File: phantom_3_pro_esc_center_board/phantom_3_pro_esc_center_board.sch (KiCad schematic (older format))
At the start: 57 parts, among them J1 CONN_BAT, J10 M1_BK, J11 M1_RD, J12 M1_YW, J13 M2_YW, J14 M2_RD, J15 M2_BK, J16 M3_BK, J17 M3_RD, J18 M3_YW, J19 M4_YW, J2 CONN_GPS, J20 M4_RD, J21 M4_BK, J3 CONN_GIMBAL, J4 CONN_CMPAS, J5 CONN_OFDM, J6 CONN_USB, J7 CONN_API, J8 CONN_MC_FRONT, J9 CONN_MC_BACK

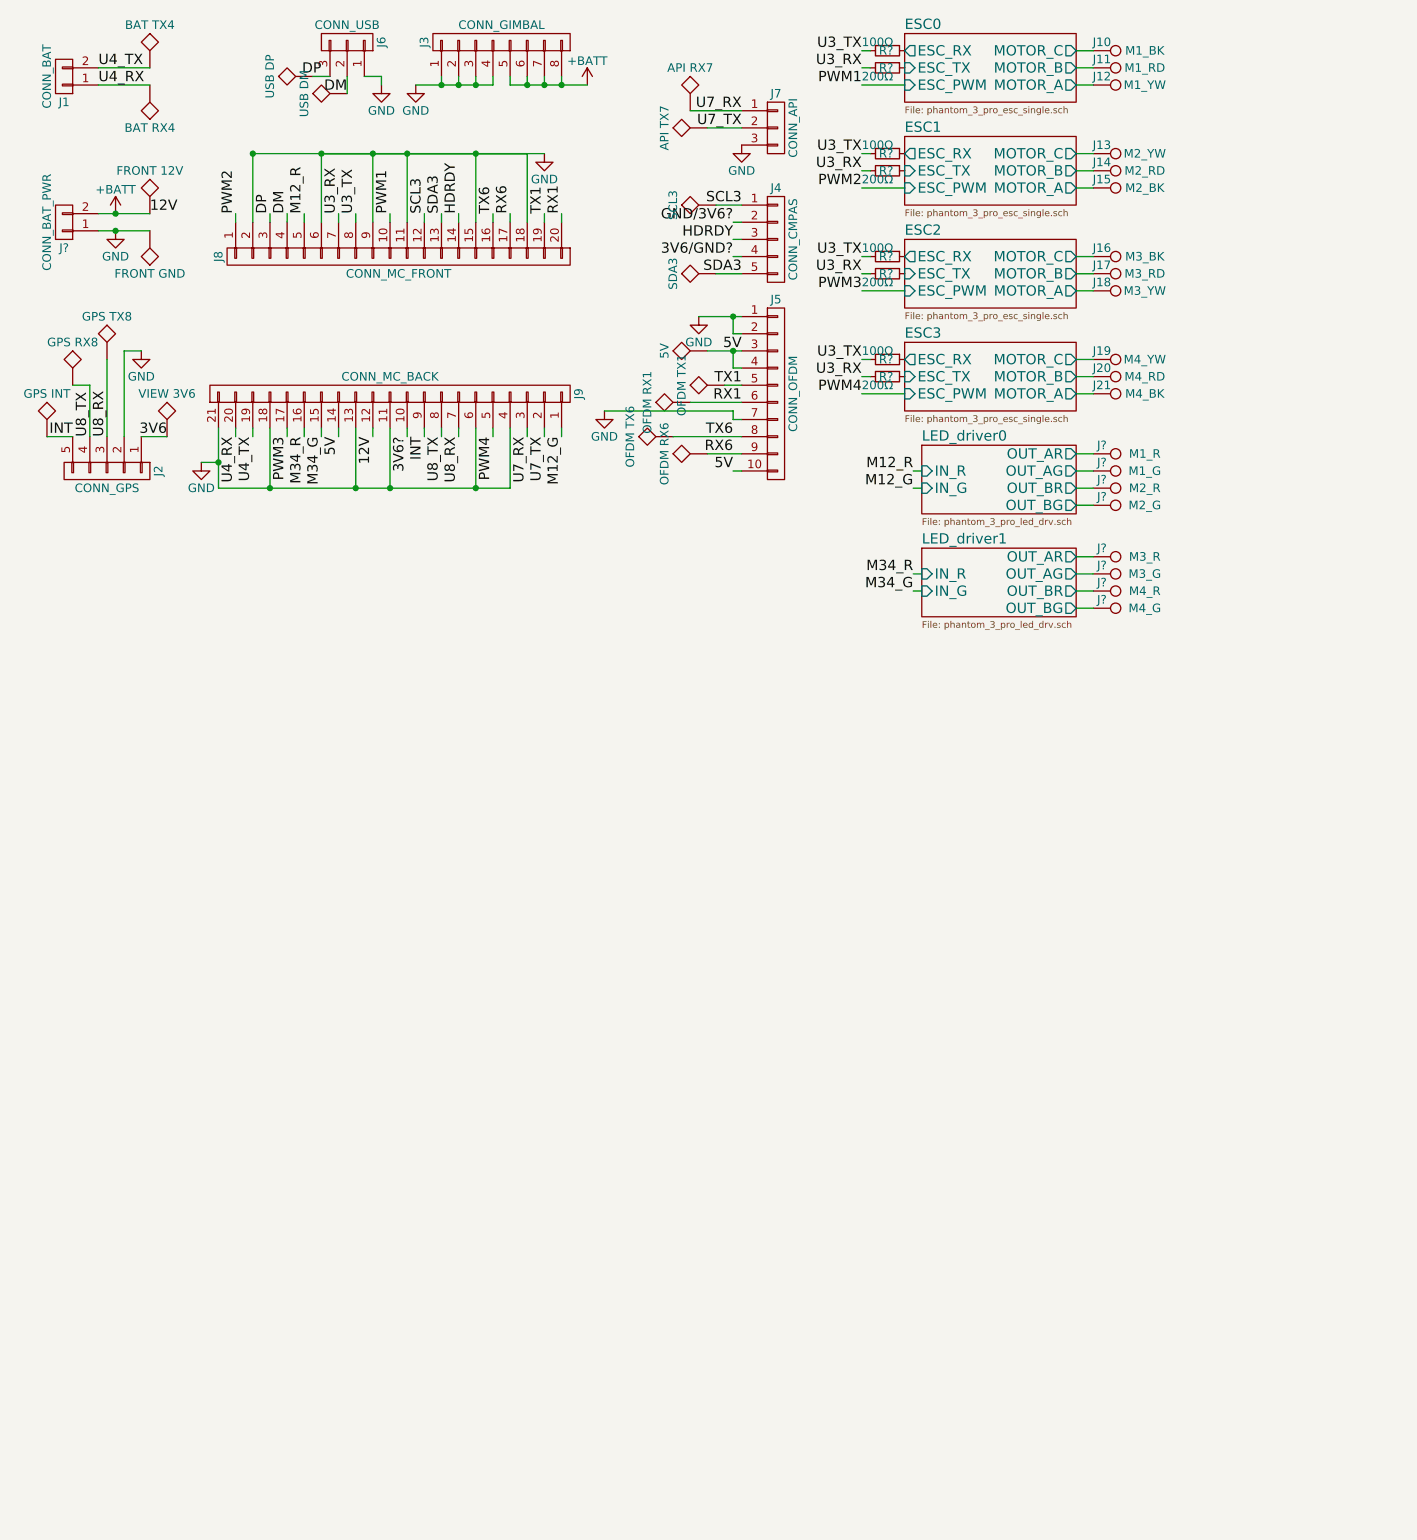
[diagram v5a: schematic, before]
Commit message: ESC Center: Added schematics of switching converters.
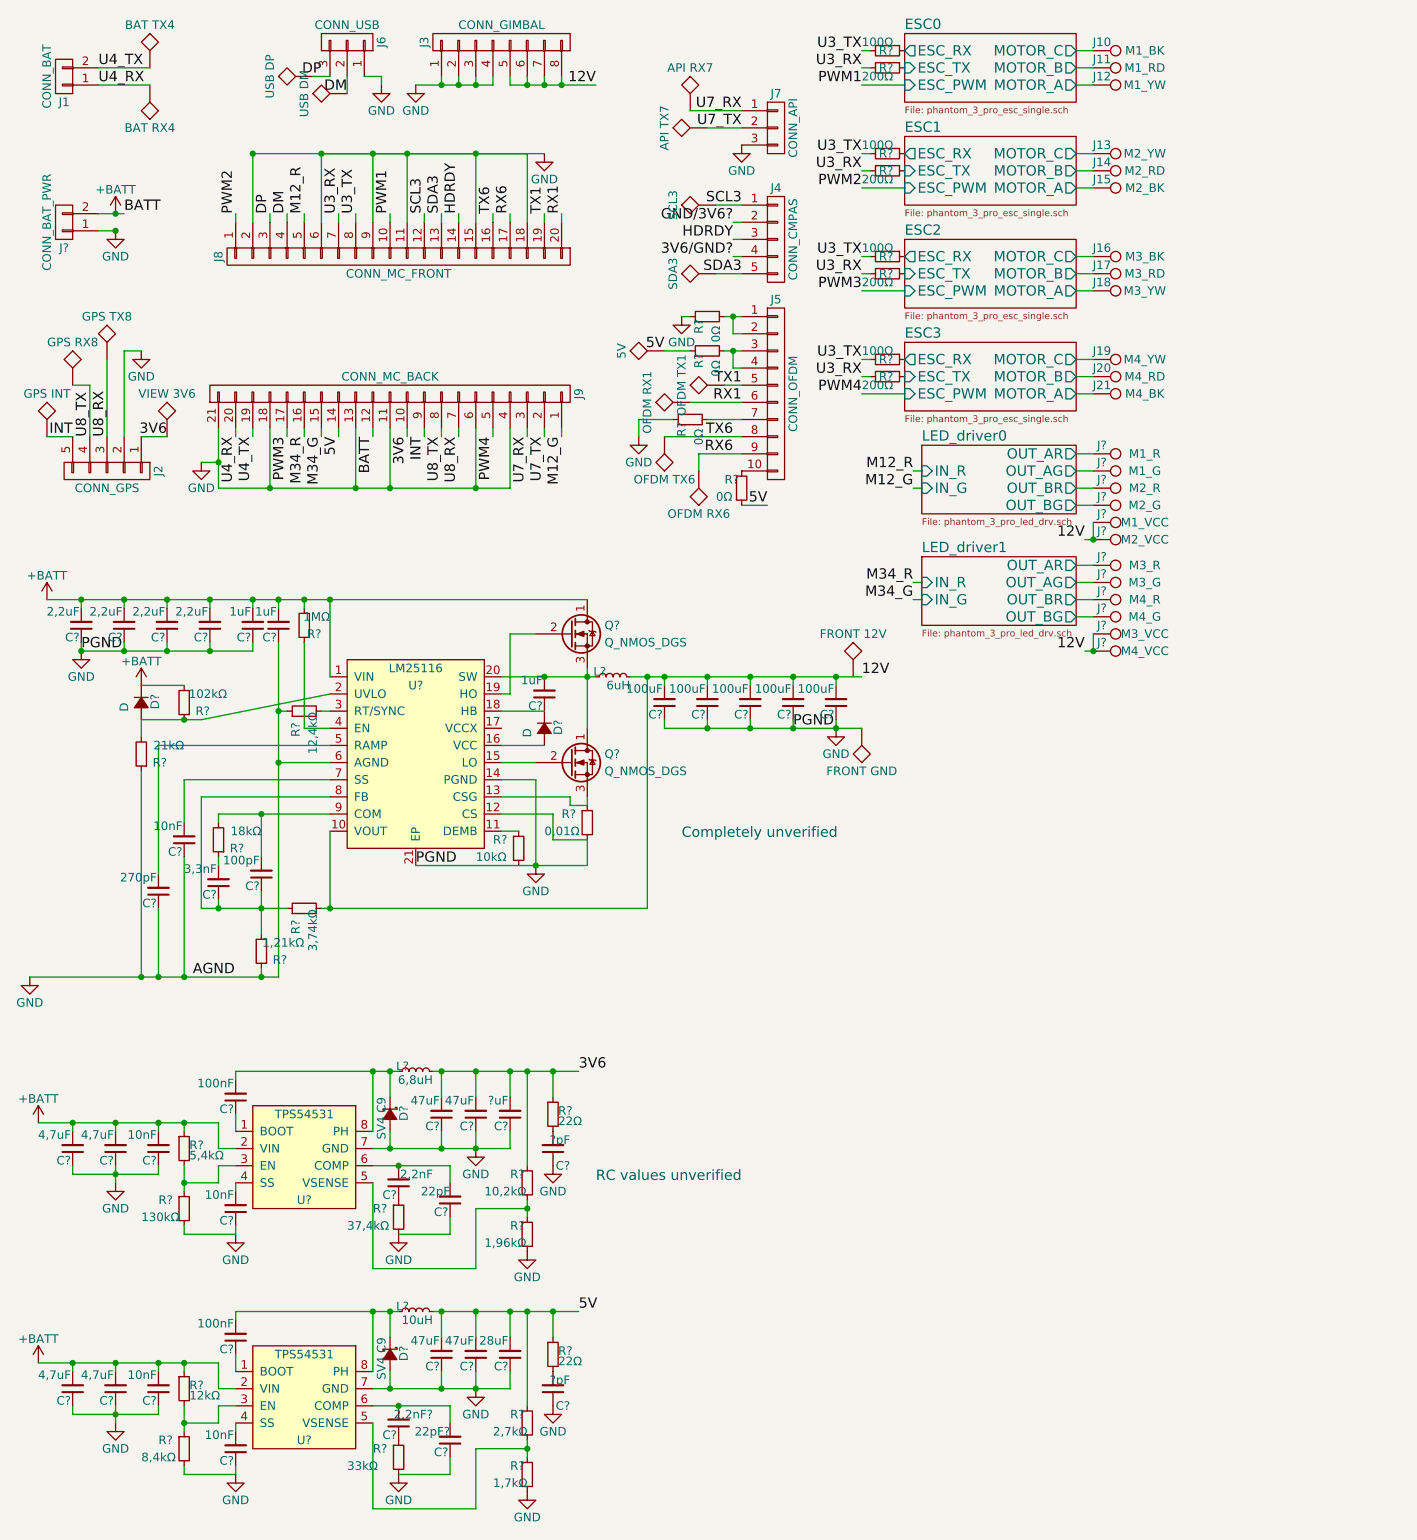
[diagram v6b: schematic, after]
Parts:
- removed TP?: FRONT 12V, symbol TEST
- removed TP?: FRONT GND, symbol TEST
- removed TP?: 5V, symbol TEST
- removed TP?: OFDM RX6, symbol TEST
- added C?: 2,2nF?, symbol C_Small
- added C? (x4): 47uF, symbol C_Small
- added C?: 28uF, symbol C_Small
- added C?: 100nF, meas. 96nF, symbol C_Small
- added C?: 10nF, meas 9.3nF, symbol C_Small
- added C? (x2): ?pF, symbol C_Small
- added C?: 22pF?, symbol C_Small
- added C? (x4): 4,7uF, symbol C_Small
- added C? (x4): 10nF, symbol C_Small
- added C? (x4): 2,2uF, symbol C_Small
- added C? (x3): 1uF, symbol C_Small
- added C? (x5): 100uF, symbol C_Small
- added C?: 100pF, symbol C_Small
- added C?: 3,3nF, symbol C_Small
- added C?: 270pF, symbol C_Small
- added C?: 2,2nF, symbol C_Small
- added C?: ?uF, symbol C_Small
- added C?: 100nF, symbol C_Small
- added C?: 22pF, symbol C_Small
- added D? (x2): SV4 C9, symbol D_Schottky_Small_ALT
- added D? (x2): D, symbol D_Small_ALT
- added J?: M1_VCC, symbol TEST_1P
- added J?: M2_VCC, symbol TEST_1P
- added J?: M3_VCC, symbol TEST_1P
- added J?: M4_VCC, symbol TEST_1P
- added L?: 10uH, symbol L_Small
- added L?: 6uH, symbol L_Small
- added L?: 6,8uH, symbol L_Small
- added Q? (x2): Q_NMOS_DGS, symbol Q_NMOS_DGS
- added R?: 12kΩ, symbol R_Small
- added R?: 8,4kΩ, symbol R_Small
- added R?: 1,7kΩ, symbol R_Small
- added R?: 2,7kΩ, symbol R_Small
- added R?: 33kΩ, symbol R_Small
- added R? (x2): 22Ω, symbol R_Small
- added R?: 1,21kΩ, symbol R_Small
- added R?: 3,74kΩ, symbol R_Small
- added R?: 18kΩ, symbol R_Small
- added R?: 1MΩ, symbol R_Small
- added R?: 12,4kΩ, symbol R_Small
- added R?: 102kΩ, symbol R_Small
- added R?: 21kΩ, symbol R_Small
- added R?: 0,01Ω, symbol R_Small
- added R?: 10kΩ, symbol R_Small
- added R?: 5,4kΩ, symbol R_Small
- added R?: 130kΩ, symbol R_Small
- added R?: 1,96kΩ, symbol R_Small
- added R?: 10,2kΩ, symbol R_Small
- added R?: 37,4kΩ, symbol R_Small
- added R? (x4): 0Ω, symbol R_Small
- added TP?: 5V, symbol TEST
- added TP?: OFDM RX6, symbol TEST
- added TP?: FRONT 12V, symbol TEST
- added TP?: FRONT GND, symbol TEST
- added U?: LM25116, symbol LM25116
- added U? (x2): TPS54531, symbol TPS54531
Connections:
- net 3V6? is gone; now on net 3V6: J9.10 (P10)
- net +BATT: now also C?.2, C?.2, C?.2, C?.2, C?.2, C?.2, C?.2, C?.2, C?.2, C?.2, C?.2, C?.2, D?.1 (K), Q?.1 (D), R?.1, R?.1, R?.2, R?.2, U?.1 (VIN), U?.2 (VIN), U?.2 (VIN); no longer J3.5 (P5), J3.6 (P6), J3.7 (P7), J3.8 (P8)
- net 3V6: now also C?.2, C?.2, C?.2, L?.2, R?.1, R?.1
- net 5V: now also C?.2, C?.2, C?.2, L?.2, R?.1, R?.1, R?.1, R?.2, TP?.1; no longer J5.10 (P10), J5.3 (P3), J5.4 (P4)
- net GND: now also C?.1, C?.1, C?.1, C?.1, C?.1, C?.1, C?.1, C?.1, C?.1, C?.1, C?.1, C?.1, C?.1, C?.1, C?.1, C?.1, C?.1, C?.1, C?.1, C?.1, C?.1, C?.1, C?.1, C?.1, C?.1, C?.1, C?.1, C?.1, C?.1, C?.1, C?.1, D?.2 (A), D?.2 (A), R?.1, R?.1, R?.1, R?.1, R?.1, R?.2, R?.2, R?.2, R?.2, R?.2, R?.2, R?.2, TP?.1, U?.12 (CS), U?.14 (PGND), U?.21 (EP), U?.6 (AGND), U?.7 (GND), U?.7 (GND); no longer J5.1 (P1), J5.2 (P2), J5.7 (P7)
- net RX6: now also TP?.1
- new net: J5.1 (P1), J5.2 (P2), R?.2
- new net: J5.10 (P10), R?.1
- new net: J5.3 (P3), J5.4 (P4), R?.2
- new net: J5.7 (P7), R?.2
- new net: R?.1, U?.11 (DEMB)
- new net: Q?.3 (S), R?.1, U?.13 (CSG)
- new net: Q?.2 (G), U?.15 (LO)
- new net: D?.2 (A), U?.16 (VCC)
- new net: C?.1, D?.1 (K), U?.18 (HB)
- new net: Q?.2 (G), U?.19 (HO)
- new net: D?.2 (A), R?.1, R?.2, U?.2 (UVLO)
- new net: C?.2, L?.1, Q?.1 (D), Q?.3 (S), U?.20 (SW)
- new net: R?.2, U?.3 (RT/SYNC)
- new net: R?.1, U?.4 (EN)
- new net: C?.2, U?.5 (RAMP)
- new net: C?.2, U?.7 (SS)
- new net: C?.1, C?.1, R?.1, R?.2, U?.8 (FB)
- new net: C?.2, R?.2, U?.9 (COM)
- new net: C?.1, U?.1 (BOOT) (x2)
- new net: R?.1, R?.2, U?.3 (EN) (x2)
- new net: C?.2, U?.4 (SS) (x2)
- new net: R?.1, R?.2, U?.5 (VSENSE) (x2)
- new net: C?.2, C?.2, U?.6 (COMP) (x2)
- new net: C?.2, D?.1 (K), L?.1, U?.8 (PH) (x2)
- new net: C?.1, R?.1 (x2)
- new net: C?.2, R?.2 (x2)
- new net: C?.2, R?.1
- new net 12V: C?.2, C?.2, C?.2, C?.2, C?.2, J3.5 (P5), J3.6 (P6), J3.7 (P7), J3.8 (P8), J?.1, J?.1, J?.1, J?.1, L?.2, R?.2, U?.10 (VOUT)
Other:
- note added: "Completely unverified"
- note added: "RC values unverified"
- moved on the sheet: J?

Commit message: Updated PDF exports.
The schematics exported to PDF were updated.
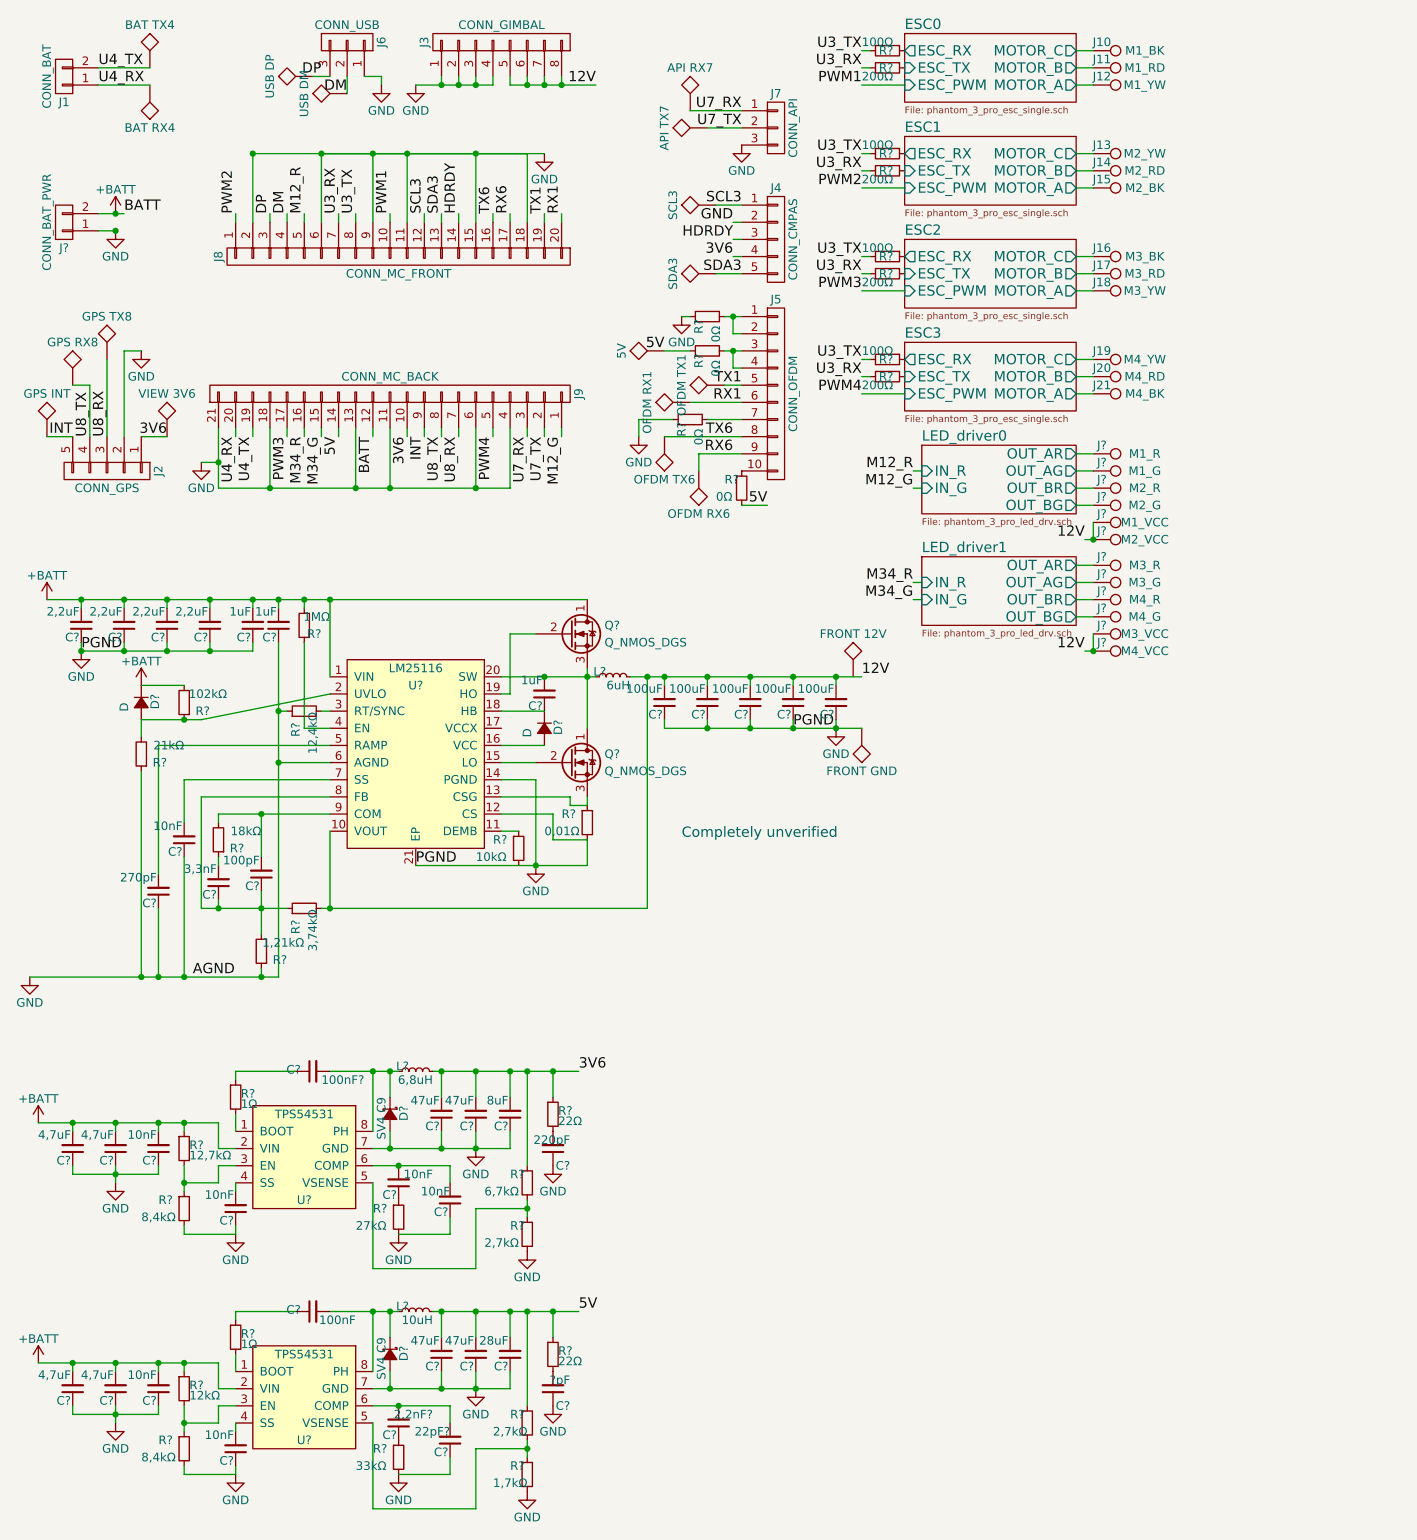
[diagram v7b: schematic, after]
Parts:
- added R? (x2): 1Ω, symbol R_Small
- C?: value 2,2nF -> 10nF
- C?: value ?uF -> 8uF
- C?: value 100nF -> 100nF?
- C?: value 22pF -> 10nF
- C?: value ?pF -> 220pF
- R?: value 5,4kΩ -> 12,7kΩ
- R?: value 130kΩ -> 8,4kΩ
- R?: value 1,96kΩ -> 2,7kΩ
- R?: value 10,2kΩ -> 6,7kΩ
- R?: value 37,4kΩ -> 27kΩ
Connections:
- net 3V6/GND? is gone; now on net 3V6: J4.4 (P4)
- net GND/3V6? is gone; now on net GND: J4.2 (P2)
- net at U?.1 (BOOT): now also R?.2; no longer C?.1
- net at C?.1: now also R?.1; no longer U?.1 (BOOT)
- new net: C?.1, R?.1
- new net: R?.2, U?.1 (BOOT)
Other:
- note removed: "RC values unverified"
- moved on the sheet: C?
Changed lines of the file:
@@
 $EndComp
 Text Label 4650 1700 2    60   ~ 0
-GND/3V6?
+GND
 Text Label 4650 1900 2    60   ~ 0
-3V6/GND?
+3V6
 $Comp
 L LM25116 U?
@@
 L C_Small C?
 U 1 1 597BBDD7
-P 1750 8200
-F 0 "C?" H 1760 8270 50  0000 L CNN
-F 1 "100nF" H 1760 8120 50  0000 L CNN
-F 2 "meas. 96nF" H 1750 8200 50  0001 C CNN
-F 3 "" H 1750 8200 50  0001 C CNN
-	1    1750 8200
-	-1   0    0    1
+P 2200 8050
+F 0 "C?" V 2210 8120 50  0000 L CNN
+F 1 "100nF" V 2150 7800 50  0000 L CNN
+F 2 "meas. 96nF" H 2200 8050 50  0001 C CNN
+F 3 "" H 2200 8050 50  0001 C CNN
+	1    2200 8050
+	0    -1   -1   0
 $EndComp
 $Comp
@@
 P 2700 8900
 F 0 "R?" H 2550 8950 50  0000 L CNN
-F 1 "33kΩ" H 2400 8850 50  0000 L CNN
+F 1 "33kΩ" H 2450 8850 50  0000 L CNN
 F 2 "" H 2700 8900 50  0001 C CNN
 F 3 "" H 2700 8900 50  0001 C CNN
@@
 	1750 8100 1750 8050
 Wire Wire Line
-	1750 8050 2700 8050
-Wire Wire Line
 	2550 8050 2550 8400
 Wire Wire Line
@@
 P 2700 7300
 F 0 "C?" H 2710 7370 50  0000 L CNN
-F 1 "2,2nF" H 2500 7250 50  0000 L CNN
+F 1 "10nF" H 2500 7250 50  0000 L CNN
 F 2 "" H 2700 7300 50  0001 C CNN
 F 3 "" H 2700 7300 50  0001 C CNN
@@
 P 3350 6900
 F 0 "C?" H 3360 6970 50  0000 L CNN
-F 1 "?uF" H 3360 6820 50  0000 L CNN
+F 1 "8uF" H 3360 6820 50  0000 L CNN
 F 2 "" H 3350 6900 50  0001 C CNN
 F 3 "" H 3350 6900 50  0001 C CNN
@@
 L C_Small C?
 U 1 1 59840470
-P 1750 6800
-F 0 "C?" H 1760 6870 50  0000 L CNN
-F 1 "100nF" H 1760 6720 50  0000 L CNN
-F 2 "" H 1750 6800 50  0001 C CNN
-F 3 "" H 1750 6800 50  0001 C CNN
-	1    1750 6800
-	-1   0    0    1
+P 2200 6650
+F 0 "C?" V 2210 6720 50  0000 L CNN
+F 1 "100nF?" V 2150 6350 50  0000 L CNN
+F 2 "" H 2200 6650 50  0001 C CNN
+F 3 "" H 2200 6650 50  0001 C CNN
+	1    2200 6650
+	0    -1   -1   0
 $EndComp
 $Comp
@@
 P 3000 7400
 F 0 "C?" H 3010 7470 50  0000 L CNN
-F 1 "22pF" H 3000 7350 50  0000 L CNN
+F 1 "10nF" H 3000 7350 50  0000 L CNN
 F 2 "" H 3000 7400 50  0001 C CNN
 F 3 "" H 3000 7400 50  0001 C CNN
@@
 P 1450 7100
 F 0 "R?" H 1480 7120 50  0000 L CNN
-F 1 "5,4kΩ" H 1480 7060 50  0000 L CNN
+F 1 "12,7kΩ" H 1480 7060 50  0000 L CNN
 F 2 "" H 1450 7100 50  0001 C CNN
 F 3 "" H 1450 7100 50  0001 C CNN
@@
 P 1450 7450
 F 0 "R?" H 1300 7500 50  0000 L CNN
-F 1 "130kΩ" H 1200 7400 50  0000 L CNN
+F 1 "8,4kΩ" H 1200 7400 50  0000 L CNN
 F 2 "" H 1450 7450 50  0001 C CNN
 F 3 "" H 1450 7450 50  0001 C CNN
@@
 P 3450 7600
 F 0 "R?" H 3350 7650 50  0000 L CNN
-F 1 "1,96kΩ" H 3200 7550 50  0000 L CNN
+F 1 "2,7kΩ" H 3200 7550 50  0000 L CNN
 F 2 "" H 3450 7600 50  0001 C CNN
 F 3 "" H 3450 7600 50  0001 C CNN
@@
 P 3450 7300
 F 0 "R?" H 3350 7350 50  0000 L CNN
-F 1 "10,2kΩ" H 3200 7250 50  0000 L CNN
+F 1 "6,7kΩ" H 3200 7250 50  0000 L CNN
 F 2 "" H 3450 7300 50  0001 C CNN
 F 3 "" H 3450 7300 50  0001 C CNN
@@
 P 2700 7500
 F 0 "R?" H 2550 7550 50  0000 L CNN
-F 1 "37,4kΩ" H 2400 7450 50  0000 L CNN
+F 1 "27kΩ" H 2450 7450 50  0000 L CNN
 F 2 "" H 2700 7500 50  0001 C CNN
 F 3 "" H 2700 7500 50  0001 C CNN
@@
 	1750 6700 1750 6650
 Wire Wire Line
-	1750 6650 2700 6650
-Wire Wire Line
 	2550 6650 2550 7000
 Wire Wire Line
@@
 P 3600 7100
 F 0 "C?" H 3500 7200 50  0000 L CNN
-F 1 "?pF" H 3500 7050 50  0000 L CNN
+F 1 "220pF" H 3500 7050 50  0000 L CNN
 F 2 "" H 3600 7100 50  0001 C CNN
 F 3 "" H 3600 7100 50  0001 C CNN
@@
 Text Label 3750 6650 0    60   ~ 0
 3V6
-Text Notes 3850 7300 0    60   ~ 0
-RC values unverified
 Text Notes 4350 5300 0    60   ~ 0
 Completely unverified
@@
 Wire Wire Line
 	6750 3550 6750 3450
+$Comp
+L R_Small R?
+U 1 1 59812B26
+P 1750 6800
+F 0 "R?" H 1780 6820 50  0000 L CNN
+F 1 "1Ω" H 1780 6760 50  0000 L CNN
+F 2 "" H 1750 6800 50  0001 C CNN
+F 3 "" H 1750 6800 50  0001 C CNN
+	1    1750 6800
+	1    0    0    -1
+$EndComp
+$Comp
+L R_Small R?
+U 1 1 59812F2A
+P 1750 8200
+F 0 "R?" H 1780 8220 50  0000 L CNN
+F 1 "1Ω" H 1780 8160 50  0000 L CNN
+F 2 "" H 1750 8200 50  0001 C CNN
+F 3 "" H 1750 8200 50  0001 C CNN
+	1    1750 8200
+	1    0    0    -1
+$EndComp
+Wire Wire Line
+	2300 8050 2700 8050
+Wire Wire Line
+	1750 8050 2100 8050
+Wire Wire Line
+	1750 6650 2100 6650
+Wire Wire Line
+	2300 6650 2700 6650
 $EndSCHEMATC
